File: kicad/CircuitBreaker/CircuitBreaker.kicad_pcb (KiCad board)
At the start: 2 copper layers, 71.6 x 27.5 mm, 59 parts, among them J1 PH2.54, J4 PH2.54, J5 downlink, J6 uplink, J7 5v, SW1 usbIAP, T1 CT104D, T2 CT104D, T3 CT104D, T4 CT104D, U1 LM324, U2 STC8H8K64U-45I-TSSOP20, U3 AP1117-33, U4 ESP-12E

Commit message: silklayers review
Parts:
- D1: value green -> grn
- D2: value blue -> blu
- J7: value 5v -> PWN-In-5v
- U2: value STC8H8K64U-45I-TSSOP20 -> STC8H8K64U
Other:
- board text added: "GND RXD TXD VCC"
- board text added: "GND TXD RXD VCC"
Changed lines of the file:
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@@
       (outputformat 1)
       (mirror false)
-      (drillshape 1)
+      (drillshape 0)
       (scaleselection 1)
-      (outputdirectory "")
+      (outputdirectory "./out/")
     )
   )
@@
       (effects (font (size 1 1) (thickness 0.15)))
     )
-    (fp_text value "blue" (at 0 1.43 90) (layer "F.SilkS")
+    (fp_text value "blu" (at 0 1.43 90) (layer "F.SilkS")
       (effects (font (size 0.7 0.7) (thickness 0.15)))
     )
@@
     (fp_line (start 1 0.625) (end -1 0.625) (layer "F.Fab") (width 0.1))
     (fp_line (start -1 -0.625) (end 1 -0.625) (layer "F.Fab") (width 0.1))
-    (pad "1" smd roundrect locked (at -0.9125 0) (size 1.025 1.4) (layers "F.Cu" "F.Paste" "F.Mask") (roundrect_rratio 0.243902)
+    (pad "1" smd roundrect locked (at -0.9125 0) (size 1.025 1.4) (layers "F.Cu" "F.Paste" "F.Mask") (roundrect_rratio 0.243902439)
       (net 7 "+5V") (pintype "passive"))
-    (pad "2" smd roundrect locked (at 0.9125 0) (size 1.025 1.4) (layers "F.Cu" "F.Paste" "F.Mask") (roundrect_rratio 0.243902)
+    (pad "2" smd roundrect locked (at 0.9125 0) (size 1.025 1.4) (layers "F.Cu" "F.Paste" "F.Mask") (roundrect_rratio 0.243902439)
       (net 8 "+3V3") (pintype "passive"))
     (model "${KICAD6_3DMODEL_DIR}/Resistor_SMD.3dshapes/R_0805_2012Metric.wrl"
@@
       (effects (font (size 1 1) (thickness 0.15)))
     )
-    (fp_text value "downlink" (at 1.778 3.302 90) (layer "F.SilkS")
-      (effects (font (size 0.7 0.7) (thickness 0.15)))
+    (fp_text value "downlink" (at 2.032 4.064 90) (layer "F.SilkS")
+      (effects (font (size 0.7 0.7) (thickness 0.15) italic))
     )
     (fp_text user "${REFERENCE}" (at 0 3 90) (layer "F.Fab") hide
@@
       (effects (font (size 1 1) (thickness 0.15)))
     )
-    (fp_text value "uplink" (at -1.778 3 90) (layer "F.SilkS")
+    (fp_text value "uplink" (at -2.286 3.81 90) (layer "F.SilkS")
       (effects (font (size 0.7 0.7) (thickness 0.125)))
     )
@@
       (effects (font (size 1 1) (thickness 0.15)))
     )
-    (fp_text value "green" (at -0.063 -1.27 90) (layer "F.SilkS")
+    (fp_text value "grn" (at -0.063 -1.27 90) (layer "F.SilkS")
       (effects (font (size 0.7 0.7) (thickness 0.15)))
     )
@@
       (effects (font (size 1 1) (thickness 0.15)))
     )
-    (fp_text value "120" (at 3.81 -0.254 90) (layer "F.SilkS")
+    (fp_text value "120" (at 3.556 0 90) (layer "F.SilkS")
       (effects (font (size 0.7 0.7) (thickness 0.15)))
     )
@@
       (effects (font (size 1 1) (thickness 0.15)))
     )
-    (fp_text value "5v" (at 0.279 -2.266) (layer "F.SilkS")
+    (fp_text value "PWN-In-5v" (at -2.007 1.544 90) (layer "F.SilkS")
       (effects (font (size 0.7 0.7) (thickness 0.15)))
     )
@@
     (fp_line (start -1 0.625) (end 1 0.625) (layer "B.Fab") (width 0.1))
     (fp_line (start -1 -0.625) (end -1 0.625) (layer "B.Fab") (width 0.1))
-    (pad "1" smd roundrect locked (at -0.9125 0 270) (size 1.025 1.4) (layers "B.Cu" "B.Paste" "B.Mask") (roundrect_rratio 0.243902)
+    (pad "1" smd roundrect locked (at -0.9125 0 270) (size 1.025 1.4) (layers "B.Cu" "B.Paste" "B.Mask") (roundrect_rratio 0.243902439)
       (net 5 "ADC3") (pintype "passive"))
-    (pad "2" smd roundrect locked (at 0.9125 0 270) (size 1.025 1.4) (layers "B.Cu" "B.Paste" "B.Mask") (roundrect_rratio 0.243902)
+    (pad "2" smd roundrect locked (at 0.9125 0 270) (size 1.025 1.4) (layers "B.Cu" "B.Paste" "B.Mask") (roundrect_rratio 0.243902439)
       (net 10 "Net-(J4-Pad1)") (pintype "passive"))
     (model "${KICAD6_3DMODEL_DIR}/Resistor_SMD.3dshapes/R_0805_2012Metric.wrl"
@@
     (fp_line (start 1 0.625) (end 1 -0.625) (layer "B.Fab") (width 0.1))
     (fp_line (start 1 -0.625) (end -1 -0.625) (layer "B.Fab") (width 0.1))
-    (pad "1" smd roundrect locked (at -0.9125 0 270) (size 1.025 1.4) (layers "B.Cu" "B.Paste" "B.Mask") (roundrect_rratio 0.243902)
+    (pad "1" smd roundrect locked (at -0.9125 0 270) (size 1.025 1.4) (layers "B.Cu" "B.Paste" "B.Mask") (roundrect_rratio 0.243902439)
       (net 23 "Net-(R15-Pad2)") (pintype "passive"))
-    (pad "2" smd roundrect locked (at 0.9125 0 270) (size 1.025 1.4) (layers "B.Cu" "B.Paste" "B.Mask") (roundrect_rratio 0.243902)
+    (pad "2" smd roundrect locked (at 0.9125 0 270) (size 1.025 1.4) (layers "B.Cu" "B.Paste" "B.Mask") (roundrect_rratio 0.243902439)
       (net 24 "Net-(R16-Pad2)") (pintype "passive"))
     (model "${KICAD6_3DMODEL_DIR}/Resistor_SMD.3dshapes/R_0805_2012Metric.wrl"
@@
     (fp_line (start 1 -0.625) (end -1 -0.625) (layer "B.Fab") (width 0.1))
     (fp_line (start 1 0.625) (end 1 -0.625) (layer "B.Fab") (width 0.1))
-    (pad "1" smd roundrect locked (at -0.9125 0 270) (size 1.025 1.4) (layers "B.Cu" "B.Paste" "B.Mask") (roundrect_rratio 0.243902)
+    (pad "1" smd roundrect locked (at -0.9125 0 270) (size 1.025 1.4) (layers "B.Cu" "B.Paste" "B.Mask") (roundrect_rratio 0.243902439)
       (net 1 "ADC0") (pintype "passive"))
-    (pad "2" smd roundrect locked (at 0.9125 0 270) (size 1.025 1.4) (layers "B.Cu" "B.Paste" "B.Mask") (roundrect_rratio 0.243902)
+    (pad "2" smd roundrect locked (at 0.9125 0 270) (size 1.025 1.4) (layers "B.Cu" "B.Paste" "B.Mask") (roundrect_rratio 0.243902439)
       (net 9 "Net-(J1-Pad1)") (pintype "passive"))
     (model "${KICAD6_3DMODEL_DIR}/Resistor_SMD.3dshapes/R_0805_2012Metric.wrl"
@@
     (fp_line (start -1 0.625) (end 1 0.625) (layer "B.Fab") (width 0.1))
     (fp_line (start -1 -0.625) (end -1 0.625) (layer "B.Fab") (width 0.1))
-    (pad "1" smd roundrect locked (at -0.9125 0 270) (size 1.025 1.4) (layers "B.Cu" "B.Paste" "B.Mask") (roundrect_rratio 0.243902)
+    (pad "1" smd roundrect locked (at -0.9125 0 270) (size 1.025 1.4) (layers "B.Cu" "B.Paste" "B.Mask") (roundrect_rratio 0.243902439)
       (net 3 "ADC1") (pintype "passive"))
-    (pad "2" smd roundrect locked (at 0.9125 0 270) (size 1.025 1.4) (layers "B.Cu" "B.Paste" "B.Mask") (roundrect_rratio 0.243902)
+    (pad "2" smd roundrect locked (at 0.9125 0 270) (size 1.025 1.4) (layers "B.Cu" "B.Paste" "B.Mask") (roundrect_rratio 0.243902439)
       (net 21 "Net-(R2-Pad2)") (pintype "passive"))
     (model "${KICAD6_3DMODEL_DIR}/Resistor_SMD.3dshapes/R_0805_2012Metric.wrl"
@@
     (fp_line (start 1 -0.625) (end -1 -0.625) (layer "B.Fab") (width 0.1))
     (fp_line (start -1 0.625) (end 1 0.625) (layer "B.Fab") (width 0.1))
-    (pad "1" smd roundrect locked (at -0.9125 0 270) (size 1.025 1.4) (layers "B.Cu" "B.Paste" "B.Mask") (roundrect_rratio 0.243902)
+    (pad "1" smd roundrect locked (at -0.9125 0 270) (size 1.025 1.4) (layers "B.Cu" "B.Paste" "B.Mask") (roundrect_rratio 0.243902439)
       (net 4 "ADC2") (pintype "passive"))
-    (pad "2" smd roundrect locked (at 0.9125 0 270) (size 1.025 1.4) (layers "B.Cu" "B.Paste" "B.Mask") (roundrect_rratio 0.243902)
+    (pad "2" smd roundrect locked (at 0.9125 0 270) (size 1.025 1.4) (layers "B.Cu" "B.Paste" "B.Mask") (roundrect_rratio 0.243902439)
       (net 22 "Net-(R3-Pad2)") (pintype "passive"))
     (model "${KICAD6_3DMODEL_DIR}/Resistor_SMD.3dshapes/R_0805_2012Metric.wrl"
@@
     (property "Sheetname" "")
     (attr smd)
-    (fp_text reference "U2" (at 0 1.524) (layer "B.SilkS")
-      (effects (font (size 1 1) (thickness 0.15)) (justify mirror))
-    )
-    (fp_text value "STC8H8K64U-45I-TSSOP20" (at 8.382 -3.0905) (layer "B.Fab")
-      (effects (font (size 1 1) (thickness 0.15)) (justify mirror))
-    )
-    (fp_text user "${REFERENCE}" (at 0 0) (layer "B.Fab")
+    (fp_text reference "U2" (at 0 1.524) (layer "B.SilkS") hide
+      (effects (font (size 1 1) (thickness 0.15)) (justify mirror))
+    )
+    (fp_text value "STC8H8K64U" (at 0 0 90) (layer "B.SilkS")
+      (effects (font (size 0.5 0.5) (thickness 0.1)) (justify mirror))
+    )
+    (fp_text user "${REFERENCE}" (at 0 0) (layer "B.Fab") hide
       (effects (font (size 1 1) (thickness 0.15)) (justify mirror))
     )
@@
   (gr_line locked (start 62 78.232) (end 111 78.232) (layer "B.SilkS") (width 0.12))
   (gr_rect locked (start 50.8 53.34) (end 122.428 80.8) (layer "Edge.Cuts") (width 0.1) (fill none))
+  (gr_text "GND\nTXD\nRXD\nVCC" (at 98.806 64.008) (layer "F.SilkS")
+    (effects (font (size 0.7 0.7) (thickness 0.15) italic))
+  )
+  (gr_text "GND\nRXD\nTXD\nVCC" (at 73.914 63.5) (layer "F.SilkS")
+    (effects (font (size 0.7 0.7) (thickness 0.15) italic))
+  )
   (segment (start 78.994 59.944) (end 77.978 59.944) (width 0.127) (layer "F.Cu") (net 1))
   (segment (start 80.01 58.928) (end 78.994 59.944) (width 0.127) (layer "F.Cu") (net 1))

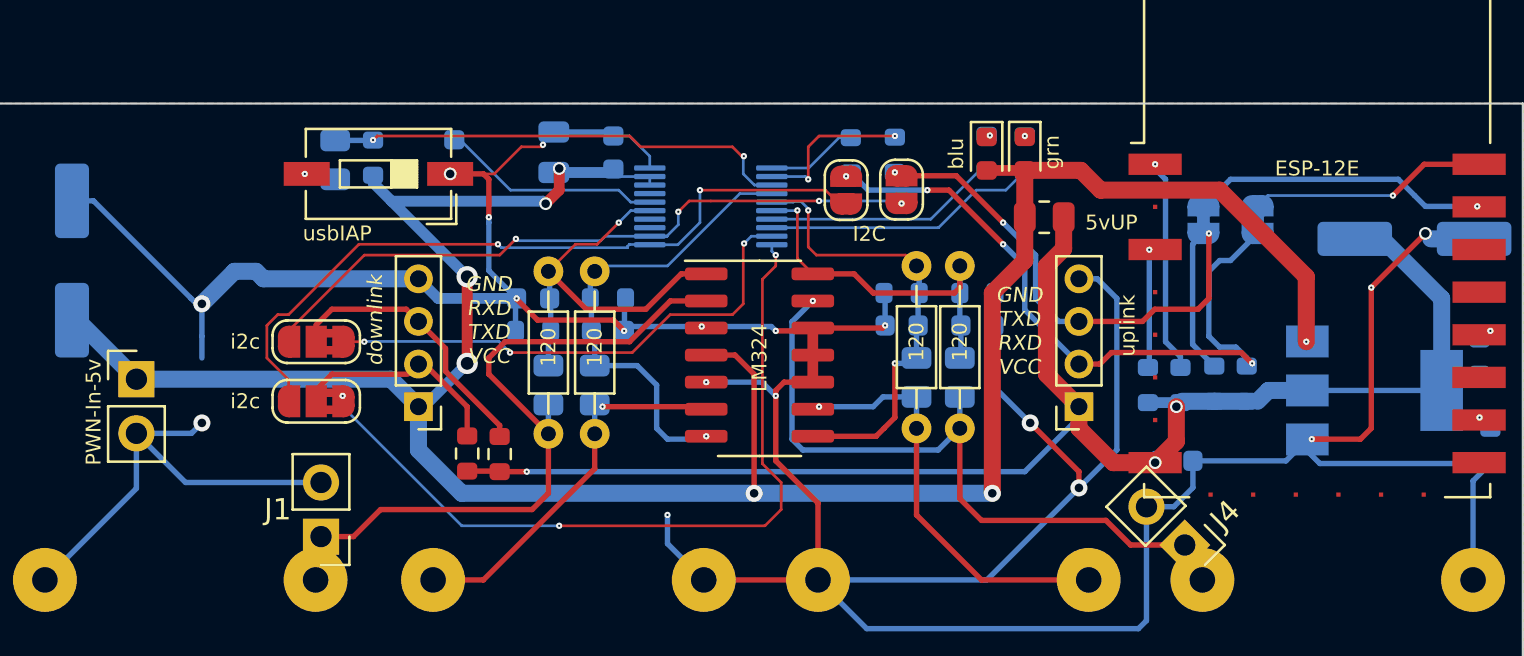
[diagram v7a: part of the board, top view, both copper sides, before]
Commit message: elimited 1.27trackwidth
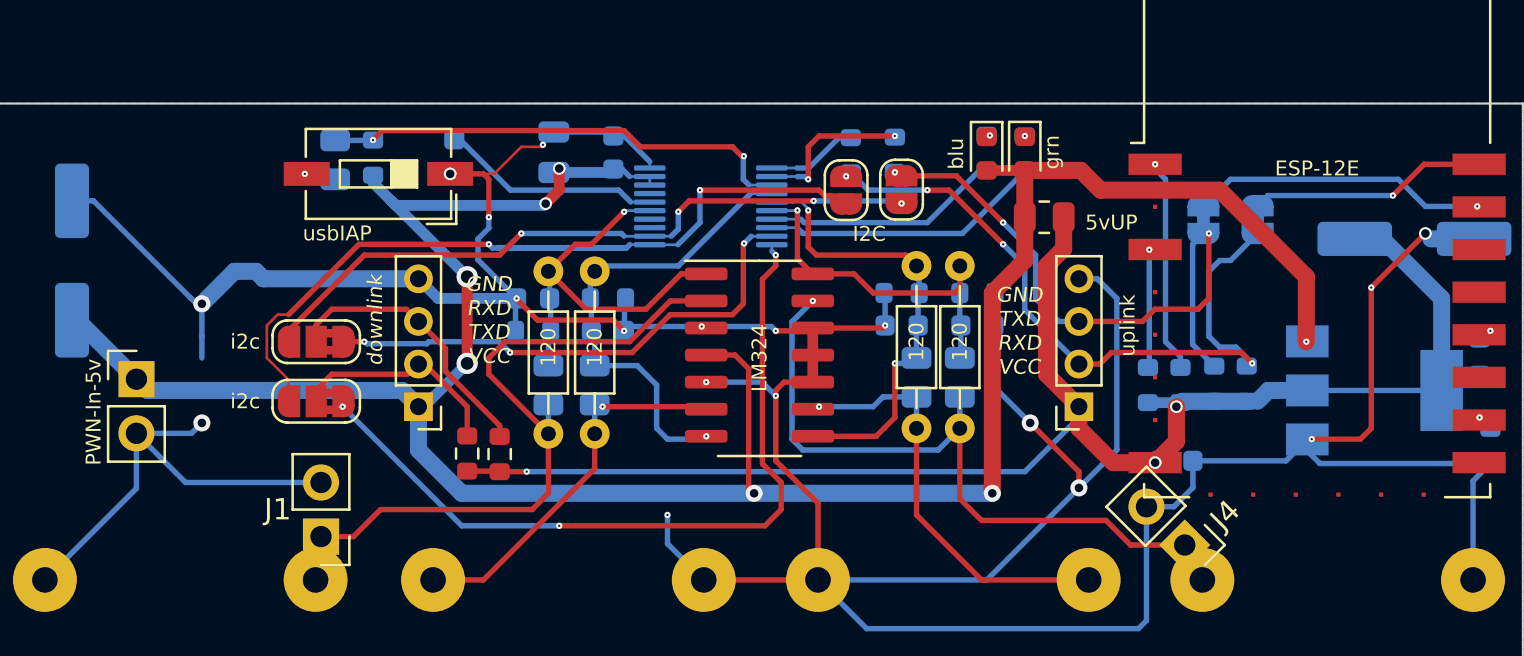
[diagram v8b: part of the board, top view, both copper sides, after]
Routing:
- net SDA: track 34.4 -> 40.5 mm
- net SCL: track 33.1 -> 32.4 mm
- net DTXD: track 36.8 -> 36.3 mm
